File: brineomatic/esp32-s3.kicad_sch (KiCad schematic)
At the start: 37 parts, among them J19 USB_TYPE_C_16PIN, J20 Conn_01x04, U5 ESP32-S3-WROOM-1-N16R8, U6 USBLC6-2SC6, U7 LDL1117S33R, U8 SN74LV1T34DBV

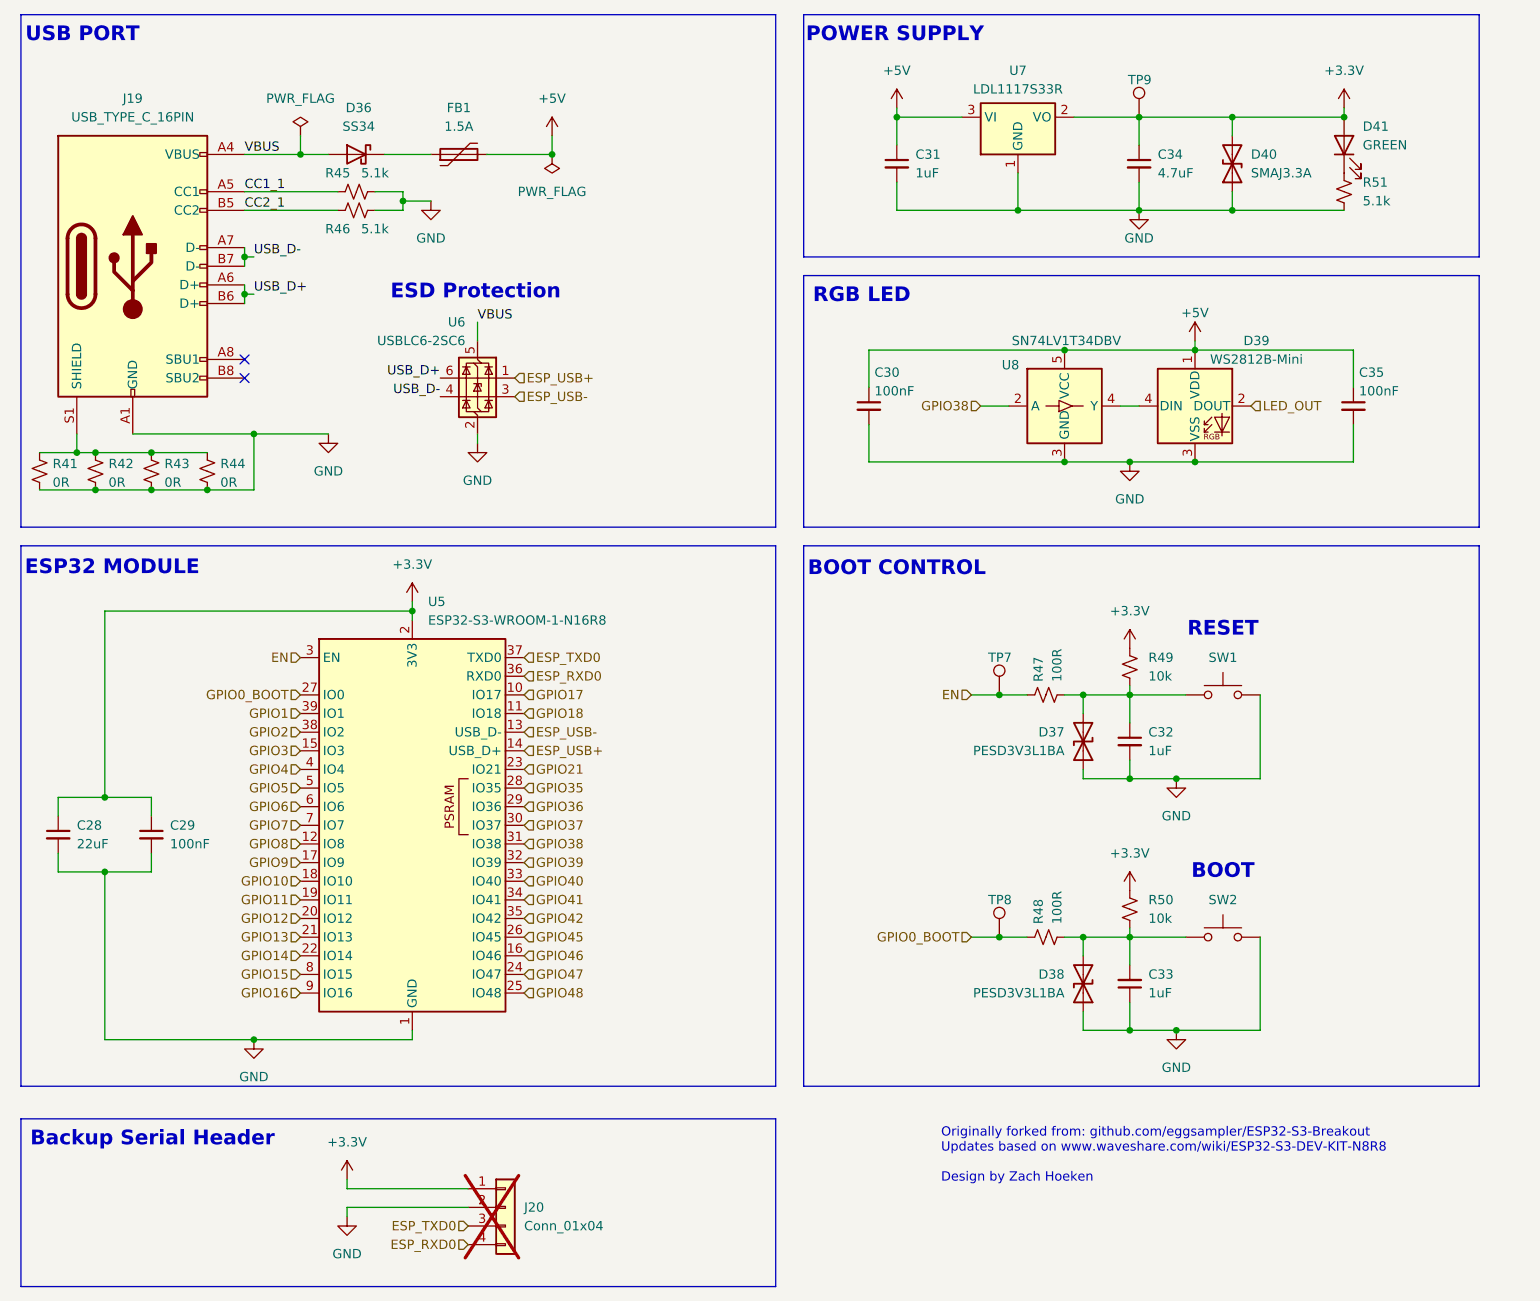
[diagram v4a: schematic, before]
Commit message: added more input/output caps
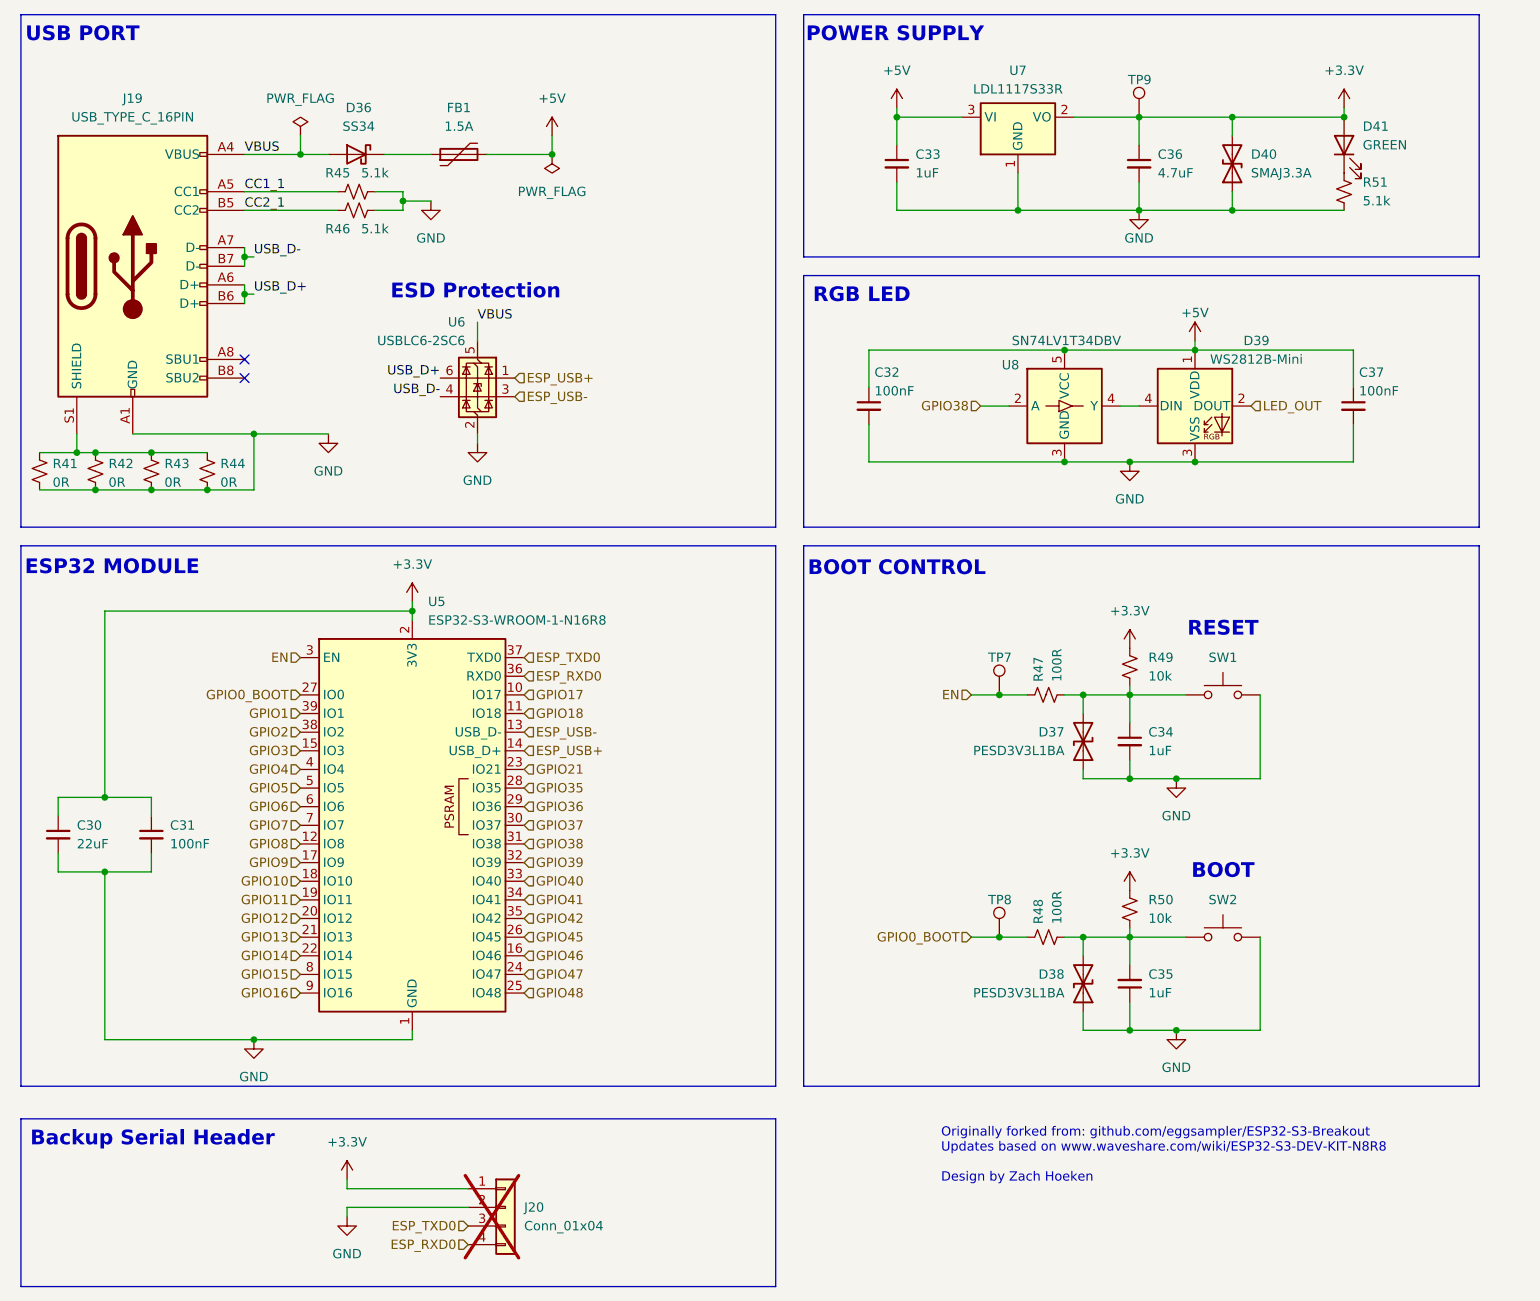
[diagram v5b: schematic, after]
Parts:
- renumbered C28 to C30, C29 to C31, C30 to C32, C31 to C33, C32 to C34, C33 to C35, C34 to C36, C35 to C37
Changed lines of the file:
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@@
 		(dnp no)
 		(fields_autoplaced yes)
-		(property "Reference" "C31"
+		(property "Reference" "C33"
 			(at 175.26 35.5662 0)
 			(effects
@@
 			(project "brineomatic"
 				(path "/96477ae2-ef08-48f3-8dd4-fe4478541f68/602af921-0504-453c-a784-e82800e98f4c"
-					(reference "C31")
+					(reference "C33")
 					(unit 1)
 				)
@@
 		(dnp no)
 		(fields_autoplaced yes)
-		(property "Reference" "C28"
+		(property "Reference" "C30"
 			(at 60.96 127.0062 0)
 			(effects
@@
 			(project "brineomatic"
 				(path "/96477ae2-ef08-48f3-8dd4-fe4478541f68/602af921-0504-453c-a784-e82800e98f4c"
-					(reference "C28")
+					(reference "C30")
 					(unit 1)
 				)
@@
 		(dnp no)
 		(fields_autoplaced yes)
-		(property "Reference" "C32"
+		(property "Reference" "C34"
 			(at 207.01 114.3062 0)
 			(effects
@@
 			(project "brineomatic"
 				(path "/96477ae2-ef08-48f3-8dd4-fe4478541f68/602af921-0504-453c-a784-e82800e98f4c"
-					(reference "C32")
+					(reference "C34")
 					(unit 1)
 				)
@@
 		(dnp no)
 		(fields_autoplaced yes)
-		(property "Reference" "C33"
+		(property "Reference" "C35"
 			(at 207.01 147.3135 0)
 			(effects
@@
 			(project "brineomatic"
 				(path "/96477ae2-ef08-48f3-8dd4-fe4478541f68/602af921-0504-453c-a784-e82800e98f4c"
-					(reference "C33")
+					(reference "C35")
 					(unit 1)
 				)
@@
 		(dnp no)
 		(fields_autoplaced yes)
-		(property "Reference" "C29"
+		(property "Reference" "C31"
 			(at 73.66 127.0062 0)
 			(effects
@@
 			(project "brineomatic"
 				(path "/96477ae2-ef08-48f3-8dd4-fe4478541f68/602af921-0504-453c-a784-e82800e98f4c"
-					(reference "C29")
+					(reference "C31")
 					(unit 1)
 				)
@@
 		(dnp no)
 		(fields_autoplaced yes)
-		(property "Reference" "C34"
+		(property "Reference" "C36"
 			(at 208.28 35.5662 0)
 			(effects
@@
 			(project "brineomatic"
 				(path "/96477ae2-ef08-48f3-8dd4-fe4478541f68/602af921-0504-453c-a784-e82800e98f4c"
-					(reference "C34")
+					(reference "C36")
 					(unit 1)
 				)
@@
 		(on_board yes)
 		(dnp no)
-		(property "Reference" "C30"
+		(property "Reference" "C32"
 			(at 169.672 65.278 0)
 			(effects
@@
 			(project "brineomatic"
 				(path "/96477ae2-ef08-48f3-8dd4-fe4478541f68/602af921-0504-453c-a784-e82800e98f4c"
-					(reference "C30")
+					(reference "C32")
 					(unit 1)
 				)
@@
 		(on_board yes)
 		(dnp no)
-		(property "Reference" "C35"
+		(property "Reference" "C37"
 			(at 235.712 65.278 0)
 			(effects
@@
 			(project "brineomatic"
 				(path "/96477ae2-ef08-48f3-8dd4-fe4478541f68/602af921-0504-453c-a784-e82800e98f4c"
-					(reference "C35")
+					(reference "C37")
 					(unit 1)
 				)

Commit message: added 1uF cap to pressure sensor connectors for esd
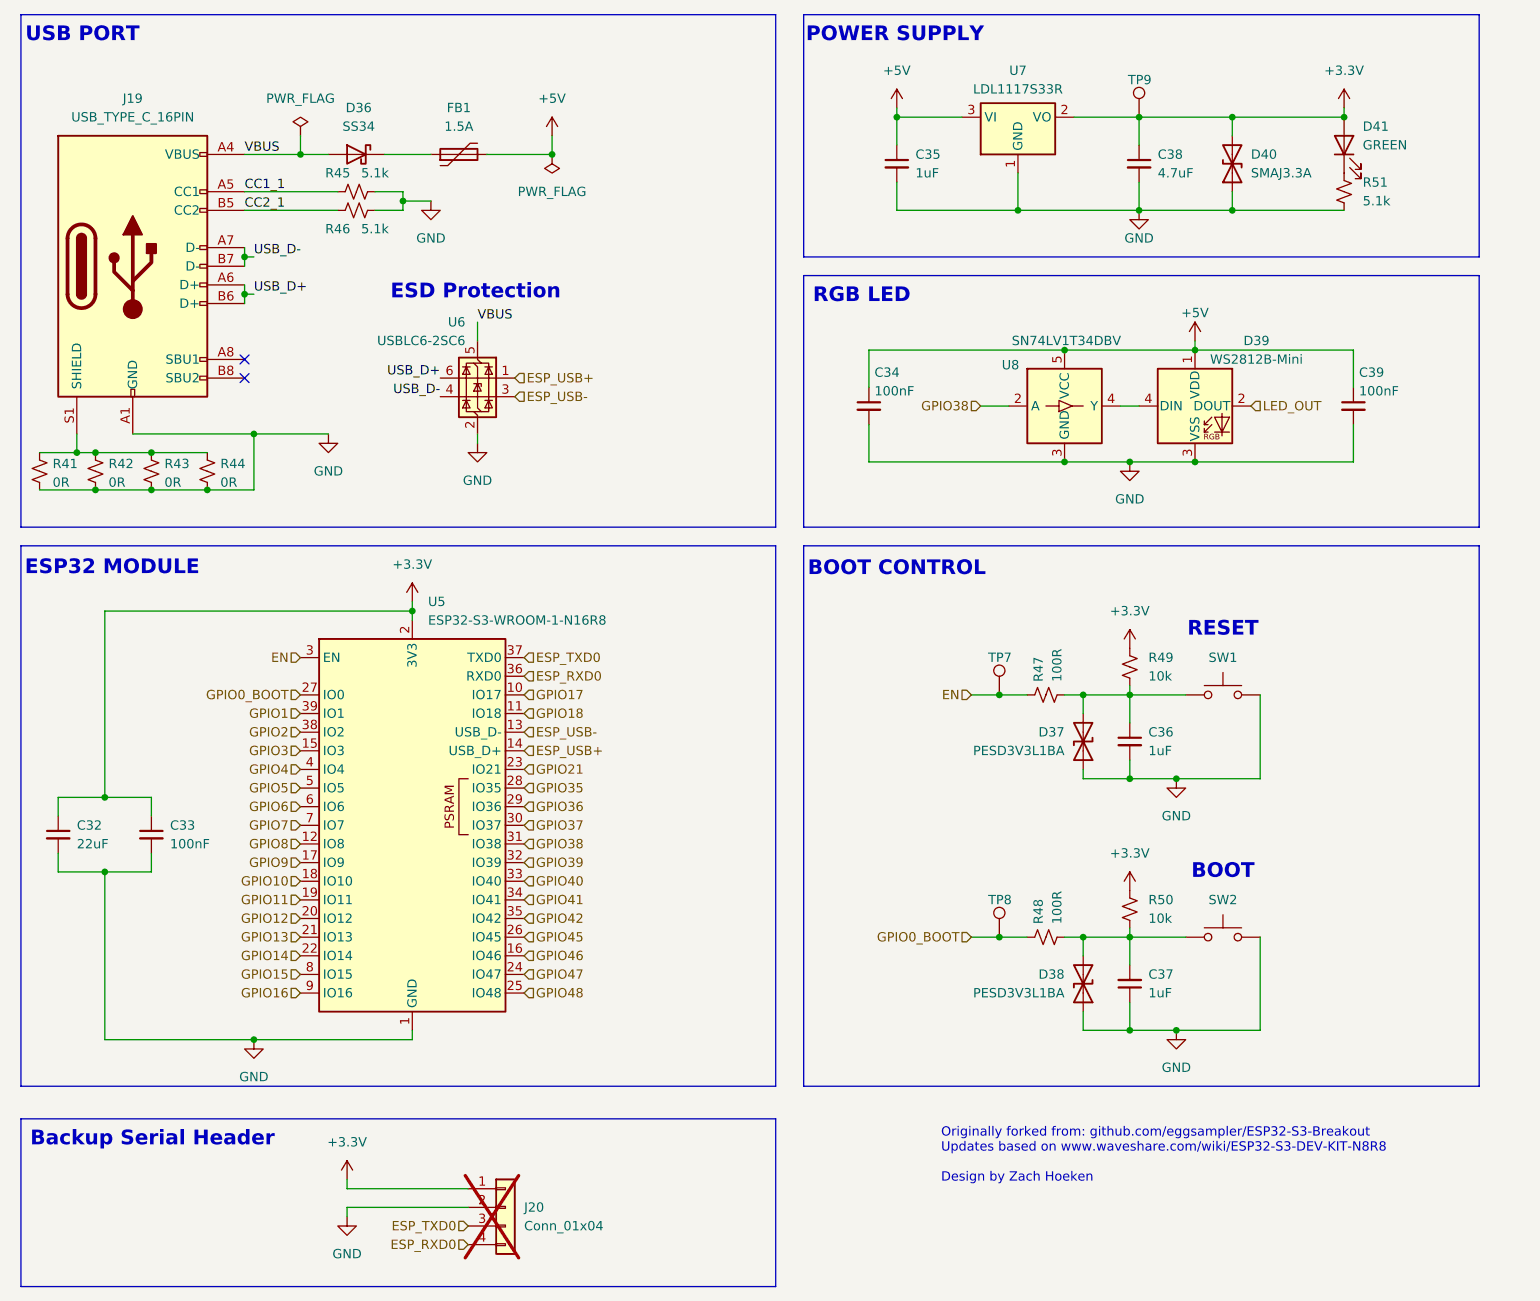
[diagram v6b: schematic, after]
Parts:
- renumbered C30 to C32, C31 to C33, C32 to C34, C33 to C35, C34 to C36, C35 to C37, C36 to C38, C37 to C39
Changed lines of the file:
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@@
 		(dnp no)
 		(fields_autoplaced yes)
-		(property "Reference" "C33"
+		(property "Reference" "C35"
 			(at 175.26 35.5662 0)
 			(effects
@@
 			(project "brineomatic"
 				(path "/96477ae2-ef08-48f3-8dd4-fe4478541f68/602af921-0504-453c-a784-e82800e98f4c"
-					(reference "C33")
+					(reference "C35")
 					(unit 1)
 				)
@@
 		(dnp no)
 		(fields_autoplaced yes)
-		(property "Reference" "C30"
+		(property "Reference" "C32"
 			(at 60.96 127.0062 0)
 			(effects
@@
 			(project "brineomatic"
 				(path "/96477ae2-ef08-48f3-8dd4-fe4478541f68/602af921-0504-453c-a784-e82800e98f4c"
-					(reference "C30")
+					(reference "C32")
 					(unit 1)
 				)
@@
 		(dnp no)
 		(fields_autoplaced yes)
-		(property "Reference" "C34"
+		(property "Reference" "C36"
 			(at 207.01 114.3062 0)
 			(effects
@@
 			(project "brineomatic"
 				(path "/96477ae2-ef08-48f3-8dd4-fe4478541f68/602af921-0504-453c-a784-e82800e98f4c"
-					(reference "C34")
+					(reference "C36")
 					(unit 1)
 				)
@@
 		(dnp no)
 		(fields_autoplaced yes)
-		(property "Reference" "C35"
+		(property "Reference" "C37"
 			(at 207.01 147.3135 0)
 			(effects
@@
 			(project "brineomatic"
 				(path "/96477ae2-ef08-48f3-8dd4-fe4478541f68/602af921-0504-453c-a784-e82800e98f4c"
-					(reference "C35")
+					(reference "C37")
 					(unit 1)
 				)
@@
 		(dnp no)
 		(fields_autoplaced yes)
-		(property "Reference" "C31"
+		(property "Reference" "C33"
 			(at 73.66 127.0062 0)
 			(effects
@@
 			(project "brineomatic"
 				(path "/96477ae2-ef08-48f3-8dd4-fe4478541f68/602af921-0504-453c-a784-e82800e98f4c"
-					(reference "C31")
+					(reference "C33")
 					(unit 1)
 				)
@@
 		(dnp no)
 		(fields_autoplaced yes)
-		(property "Reference" "C36"
+		(property "Reference" "C38"
 			(at 208.28 35.5662 0)
 			(effects
@@
 			(project "brineomatic"
 				(path "/96477ae2-ef08-48f3-8dd4-fe4478541f68/602af921-0504-453c-a784-e82800e98f4c"
-					(reference "C36")
+					(reference "C38")
 					(unit 1)
 				)
@@
 		(on_board yes)
 		(dnp no)
-		(property "Reference" "C32"
+		(property "Reference" "C34"
 			(at 169.672 65.278 0)
 			(effects
@@
 			(project "brineomatic"
 				(path "/96477ae2-ef08-48f3-8dd4-fe4478541f68/602af921-0504-453c-a784-e82800e98f4c"
-					(reference "C32")
+					(reference "C34")
 					(unit 1)
 				)
@@
 		(on_board yes)
 		(dnp no)
-		(property "Reference" "C37"
+		(property "Reference" "C39"
 			(at 235.712 65.278 0)
 			(effects
@@
 			(project "brineomatic"
 				(path "/96477ae2-ef08-48f3-8dd4-fe4478541f68/602af921-0504-453c-a784-e82800e98f4c"
-					(reference "C37")
+					(reference "C39")
 					(unit 1)
 				)
